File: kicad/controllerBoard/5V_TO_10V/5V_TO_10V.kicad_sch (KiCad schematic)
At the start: 35 parts, among them Q1 PMOS, Q636 PMOS, Q637 NMOS, Q638 NMOS, Q639 PMOS, Q640 NMOS, Q641 PMOS, Q642 NMOS, Q643 PMOS, Q644 NMOS, Q645 PMOS, Q646 NMOS, Q647 PMOS, Q648 NMOS

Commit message: did more simulation, added bom
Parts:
- removed D2: MUR1560F, Diode_THT:D_DO-35_SOD27_P7.62mm_Horizontal, symbol Device:D
- added D13, D14, D15, D16, D5: MUR1560FAC, Diode_THT:D_DO-35_SOD27_P7.62mm_Horizontal, symbol Device:D
- C16: renamed from C6; value 10mC -> 1mC
- D10, D11, D12, D7, D8, D9: value MUR1560F -> MUR1560FAC
- D6: renamed from D1; value MUR1560F -> MUR1560FAC
- renumbered C1 to C11, C2 to C12, C3 to C13, C4 to C14, C5 to C15, Q1 to Q635, R1 to R51, R2 to R52, R3 to R53, R4 to R54, R5 to R55, R6 to R56
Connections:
- net 10V: now also D16.1 (K); no longer D11.1 (K), D12.1 (K)
- net at D7.1 (K), D9.2 (A): no longer C14.1
- net at C12.1, D6.1 (K): now also D8.2 (A); no longer D7.2 (A)
- net at D10.2 (A), D8.1 (K): now also C14.1; no longer C15.1
- net at C13.1: no longer D8.2 (A)
- new net: D11.1 (K), D13.2 (A)
- new net: D12.1 (K), D14.2 (A)
- new net: D14.1 (K), D16.2 (A)
- new net: D5.1 (K), D7.2 (A)
- new net: D13.1 (K), D15.2 (A)
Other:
- moved on the sheet: C16

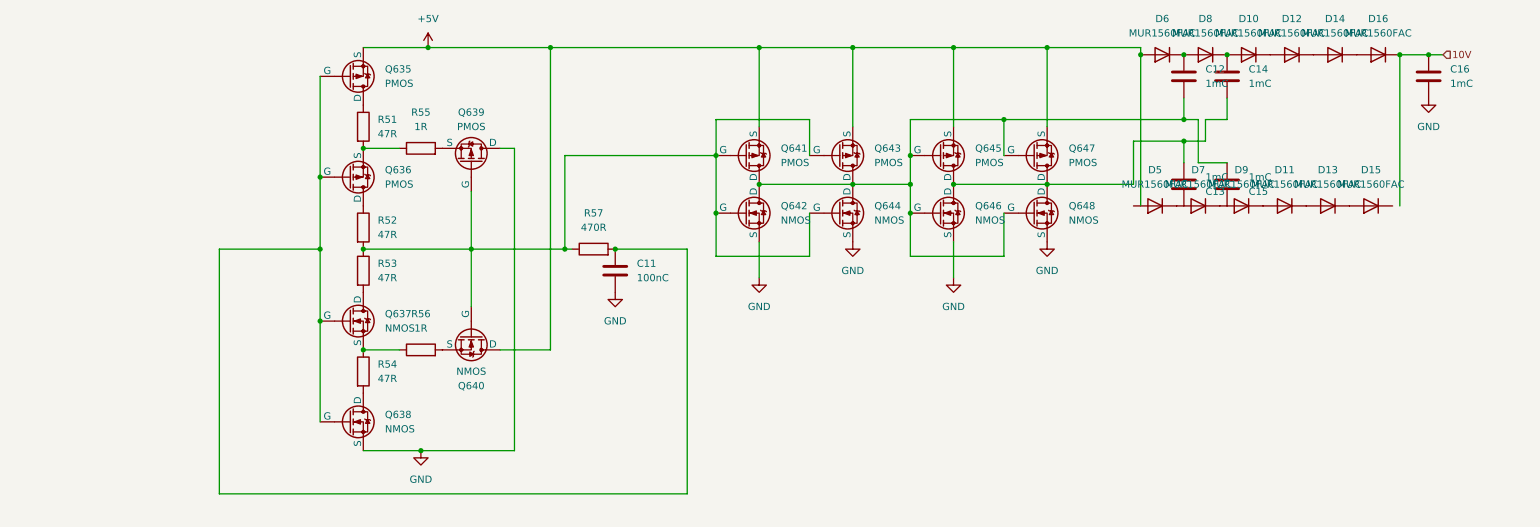
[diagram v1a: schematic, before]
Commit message: update main board schematic
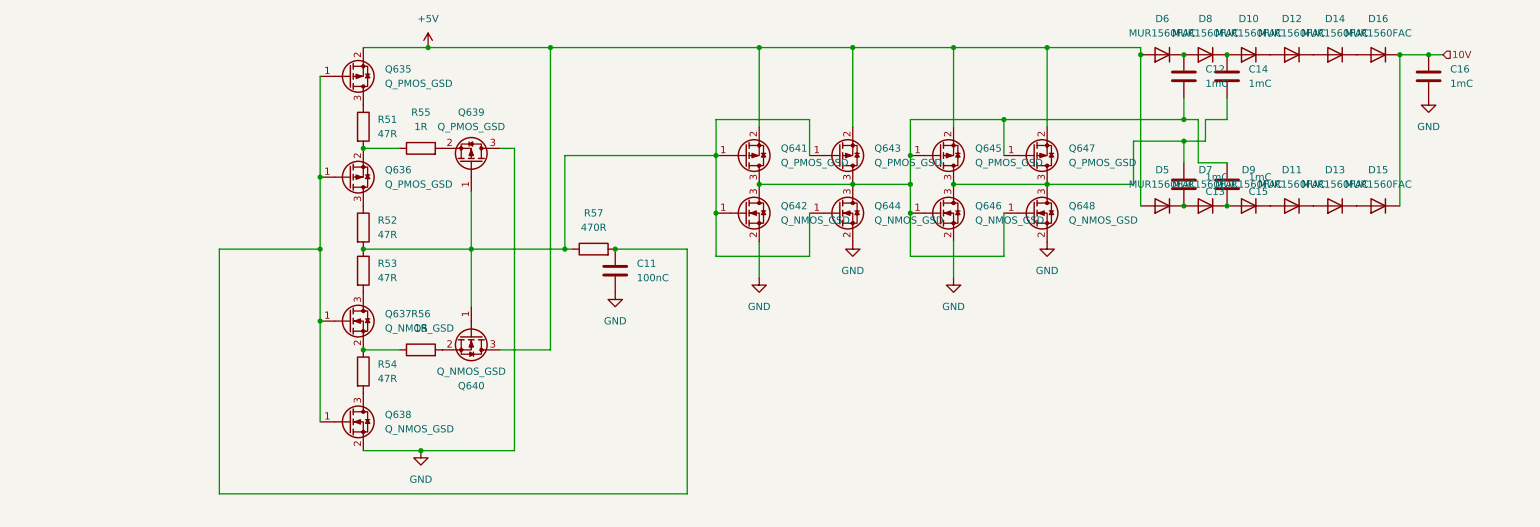
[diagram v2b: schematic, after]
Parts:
- C11: footprint (none) -> Capacitor_SMD:C_0805_2012Metric
- C12, C13, C14, C15, C16: footprint (none) -> Capacitor_THT:CP_Radial_D10.0mm_P5.00mm
- D10, D11, D12, D13, D14, D15, D16, D5, D6, D7, D8, D9: footprint Diode_THT:D_DO-35_SOD27_P7.62mm_Horizontal -> Package_TO_SOT_THT:TO-220-2_Vertical
- Q635, Q636, Q639, Q641, Q643, Q645, Q647: value PMOS -> Q_PMOS_GSD; footprint Package_DIP:DIP-24_W7.62mm -> easyeda2kicad:SOT-23-P; symbol Simulation_SPICE:PMOS -> Transistor_FET:Q_PMOS_GSD
- Q637, Q638, Q640, Q642, Q644, Q646, Q648: value NMOS -> Q_NMOS_GSD; footprint (none) -> easyeda2kicad:SOT-23-N; symbol Simulation_SPICE:NMOS -> Transistor_FET:Q_NMOS_GSD
- R51, R52, R53, R54, R55, R56, R57: footprint (none) -> Resistor_SMD:R_0805_2012Metric
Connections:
- net +5V: now also D5.2 (A), Q635.2 (S), Q640.3 (D), Q641.2 (S), Q643.2 (S), Q645.2 (S), Q647.2 (S); no longer Q635.3 (S), Q640.1 (D), Q641.3 (S), Q643.3 (S), Q645.3 (S), Q647.3 (S)
- net 10V: now also D15.1 (K)
- net GND: now also Q638.2 (S), Q639.3 (D), Q642.2 (S), Q644.2 (S), Q646.2 (S), Q648.2 (S); no longer Q638.3 (S), Q639.1 (D), Q642.3 (S), Q644.3 (S), Q646.3 (S), Q648.3 (S)
- net at Q645.1 (G), Q646.1 (G), Q647.1 (G)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: now also C12.2, C15.2, Q641.3 (D), Q642.3 (D), Q643.3 (D), Q644.3 (D); no longer C13.2, C14.2
- net at R54.1, R56.1: now also Q637.2 (S); no longer Q637.3 (S)
- net at R56.2: now also Q640.2 (S); no longer Q640.3 (S)
- net at Q636.1 (G): now also C11.1, Q635.1 (G), Q637.1 (G), Q638.1 (G), R57.2; no longer R52.1
- net at R51.2, R55.1: now also Q636.2 (S); no longer Q636.3 (S)
- net at R51.1: now also Q635.3 (D); no longer Q635.1 (D)
- net at R55.2: now also Q639.2 (S); no longer Q639.3 (S)
- net at C15.1: now also D7.1 (K), D9.2 (A)
- net at C13.1: now also D5.1 (K), D7.2 (A)
- net at R53.2: now also Q637.3 (D); no longer Q637.1 (D)
- net at R54.2: now also Q638.3 (D); no longer Q638.1 (D)
- new net: C13.2, C14.2, Q645.3 (D), Q646.3 (D), Q647.3 (D), Q648.3 (D)
- new net: Q639.1 (G), Q640.1 (G), Q641.1 (G), Q642.1 (G), Q643.1 (G), Q644.1 (G), R52.2, R53.1, R57.1
- new net: Q636.3 (D), R52.1
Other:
- moved on the sheet: D11, D13, D15, D5, D7, D9

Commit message: routed charge pump
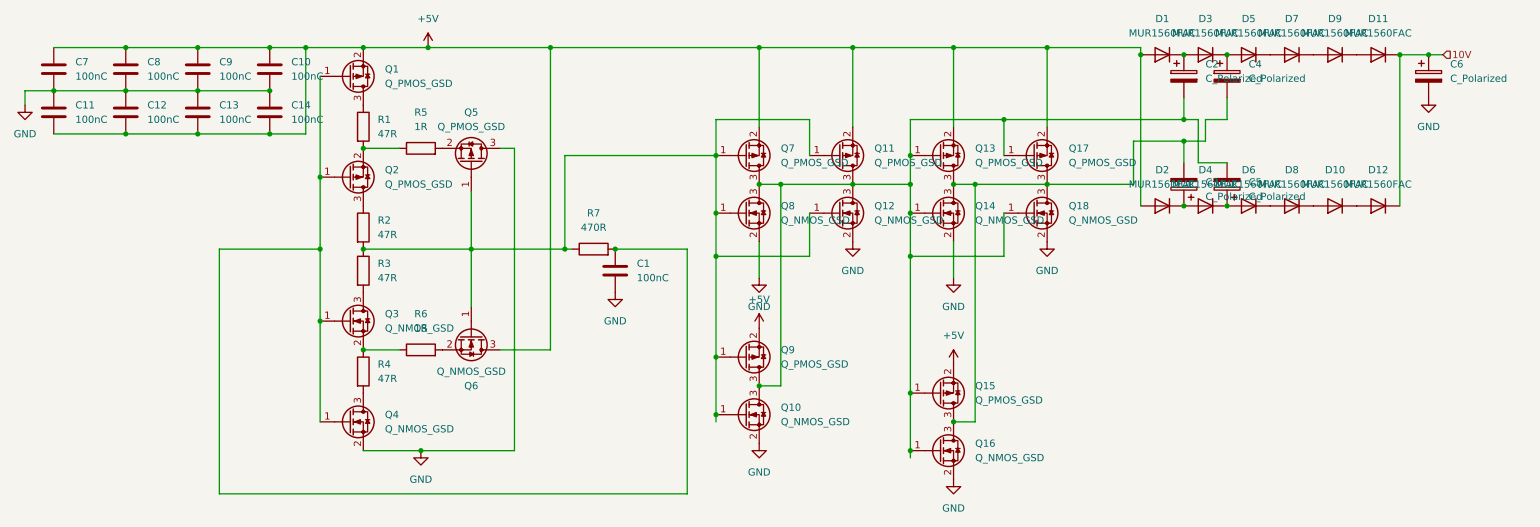
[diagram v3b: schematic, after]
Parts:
- removed C15, C16: 1mC, Capacitor_THT:CP_Radial_D10.0mm_P5.00mm, symbol Device:C
- added C10, C11, C7, C8, C9: 100nC, Capacitor_SMD:C_0805_2012Metric, symbol Device:C
- added C2, C3, C4, C5, C6: C_Polarized, Capacitor_THT:CP_Radial_D10.0mm_P5.00mm, symbol Device:C_Polarized
- added Q10, Q16: Q_NMOS_GSD, easyeda2kicad:SOT-23-N, symbol Transistor_FET:Q_NMOS_GSD
- added Q15, Q9: Q_PMOS_GSD, easyeda2kicad:SOT-23-P, symbol Transistor_FET:Q_PMOS_GSD
- C12, C13, C14: value 1mC -> 100nC; footprint Capacitor_THT:CP_Radial_D10.0mm_P5.00mm -> Capacitor_SMD:C_0805_2012Metric
- renumbered C11 to C1, D6 to D1, D13 to D10, D16 to D11, D15 to D12, D5 to D2, D8 to D3, D7 to D4, D10 to D5, D9 to D6, D12 to D7, D11 to D8, D14 to D9, Q635 to Q1, Q643 to Q11, Q644 to Q12, Q645 to Q13, Q646 to Q14, Q647 to Q17, Q648 to Q18, Q636 to Q2, Q637 to Q3, Q638 to Q4, Q639 to Q5, Q640 to Q6, Q641 to Q7, Q642 to Q8, R51 to R1, R52 to R2, R53 to R3, R54 to R4, R55 to R5, R56 to R6, R57 to R7
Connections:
- net +5V: now also C12.2, C13.2, C14.2, C10.1, C11.2, C7.1, C8.1, C9.1, Q15.2 (S), Q9.2 (S)
- net 10V: now also C6.1
- net GND: now also C12.1, C13.1, C14.1, C10.2, C11.1, C6.2, C7.2, C8.2, C9.2, Q10.2 (S), Q16.2 (S)
- net at Q11.3 (D), Q12.3 (D), Q13.1 (G)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: now also C2.2, C5.2, Q10.3 (D), Q15.1 (G), Q16.1 (G), Q9.3 (D); no longer C12.2
- net at Q13.3 (D), Q14.3 (D), Q17.3 (D)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: now also C3.2, C4.2, Q15.3 (D), Q16.3 (D); no longer C13.2, C14.2
- net at Q11.1 (G), Q12.1 (G), Q5.1 (G)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: now also Q10.1 (G), Q9.1 (G)
- net at D1.1 (K), D3.2 (A): now also C2.1; no longer C12.1
- net at D4.1 (K), D6.2 (A): now also C5.1
- net at D3.1 (K), D5.2 (A): now also C4.1; no longer C14.1
- net at D2.1 (K), D4.2 (A): now also C3.1; no longer C13.1

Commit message: finished routing all sub schematics
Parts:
- renumbered C7 to C17, C11 to C18, C8 to C19, C12 to C20, C9 to C21, C13 to C22, C10 to C23, C14 to C24, C1 to C25, C2 to C26, C3 to C27, C4 to C28, C5 to C29, C6 to C30, D6 to D10, D7 to D11, D8 to D12, D9 to D13, D10 to D14, D11 to D15, D12 to D16, D1 to D5, D2 to D6, D3 to D7, D4 to D8, D5 to D9, Q1 to Q635, Q2 to Q636, Q3 to Q637, Q4 to Q638, Q5 to Q639, Q6 to Q640, Q7 to Q641, Q8 to Q642, Q9 to Q643, Q10 to Q644, Q11 to Q645, Q12 to Q646, Q13 to Q647, Q14 to Q648, Q15 to Q649, Q16 to Q650, Q17 to Q651, Q18 to Q652, R1 to R51, R2 to R52, R3 to R53, R4 to R54, R5 to R55, R6 to R56, R7 to R57

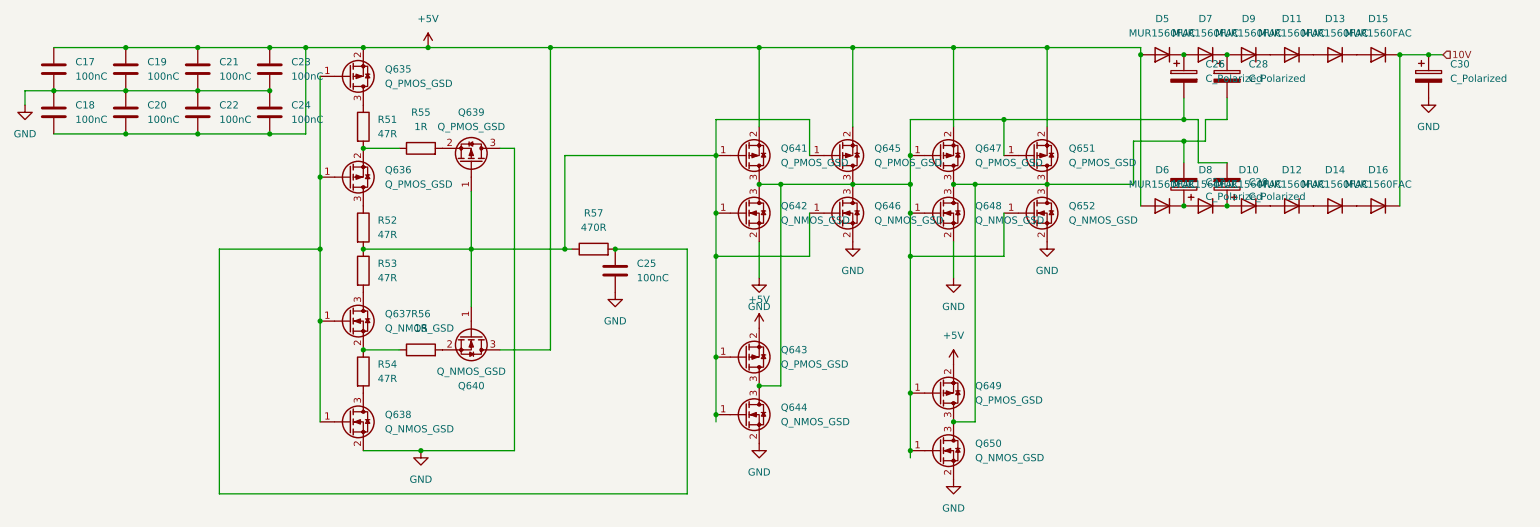
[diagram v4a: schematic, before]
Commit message: add mounting holes
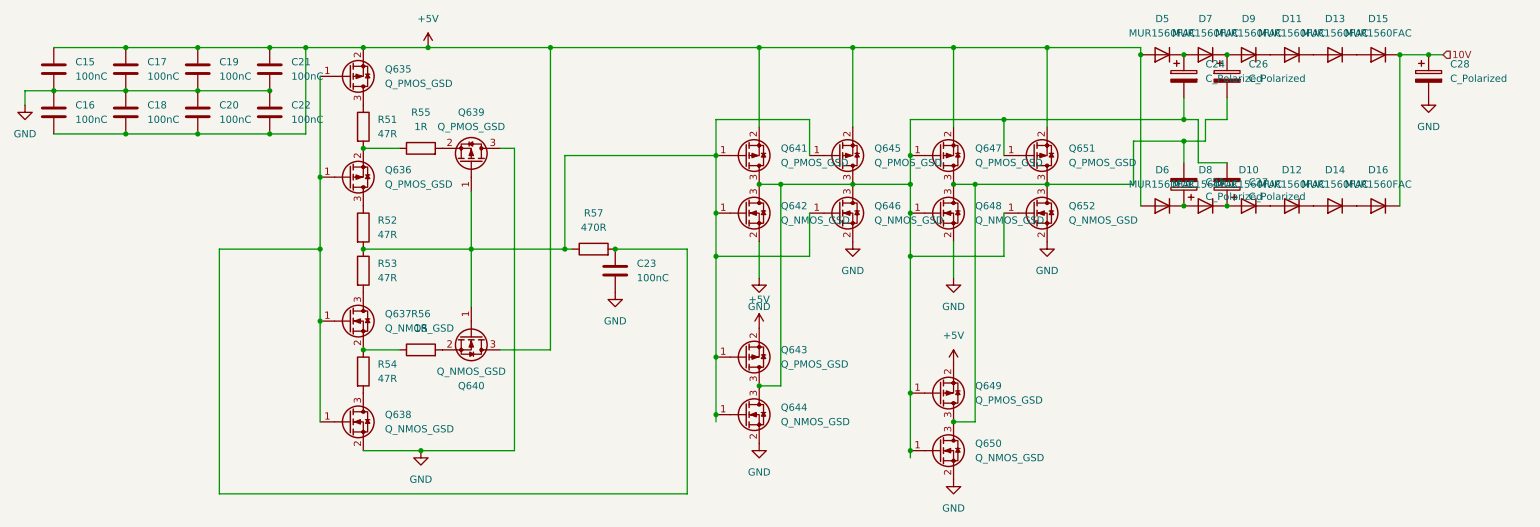
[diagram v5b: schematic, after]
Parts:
- renumbered C17 to C15, C18 to C16, C19 to C17, C20 to C18, C21 to C19, C22 to C20, C23 to C21, C24 to C22, C25 to C23, C26 to C24, C27 to C25, C28 to C26, C29 to C27, C30 to C28
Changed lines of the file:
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@@
 		(dnp no)
 		(fields_autoplaced yes)
-		(property "Reference" "#PWR0136"
+		(property "Reference" "#PWR0218"
 			(at 85.09 119.38 0)
 			(hide yes)
@@
 			(project "controllerBoard"
 				(path "/93a9a1ca-4ee5-40da-ab67-92836146c003/ba89c823-0b97-4162-9c8c-b0bfe5b1c3f2"
-					(reference "#PWR0136")
+					(reference "#PWR0218")
 					(unit 1)
 				)
@@
 		(dnp no)
 		(fields_autoplaced yes)
-		(property "Reference" "C23"
+		(property "Reference" "C21"
 			(at 62.23 44.4499 0)
 			(show_name no)
@@
 			(project "controllerBoard"
 				(path "/93a9a1ca-4ee5-40da-ab67-92836146c003/ba89c823-0b97-4162-9c8c-b0bfe5b1c3f2"
-					(reference "C23")
+					(reference "C21")
 					(unit 1)
 				)
@@
 		(dnp no)
 		(fields_autoplaced yes)
-		(property "Reference" "C30"
+		(property "Reference" "C28"
 			(at 266.7 44.8309 0)
 			(show_name no)
@@
 			(project "controllerBoard"
 				(path "/93a9a1ca-4ee5-40da-ab67-92836146c003/ba89c823-0b97-4162-9c8c-b0bfe5b1c3f2"
-					(reference "C30")
+					(reference "C28")
 					(unit 1)
 				)
@@
 		(dnp no)
 		(fields_autoplaced yes)
-		(property "Reference" "C25"
+		(property "Reference" "C23"
 			(at 123.19 80.0099 0)
 			(show_name no)
@@
 			(project "controllerBoard"
 				(path "/93a9a1ca-4ee5-40da-ab67-92836146c003/ba89c823-0b97-4162-9c8c-b0bfe5b1c3f2"
-					(reference "C25")
+					(reference "C23")
 					(unit 1)
 				)
@@
 		(dnp no)
 		(fields_autoplaced yes)
-		(property "Reference" "#PWR0146"
+		(property "Reference" "#PWR0228"
 			(at 195.58 82.55 0)
 			(hide yes)
@@
 			(project "controllerBoard"
 				(path "/93a9a1ca-4ee5-40da-ab67-92836146c003/ba89c823-0b97-4162-9c8c-b0bfe5b1c3f2"
-					(reference "#PWR0146")
+					(reference "#PWR0228")
 					(unit 1)
 				)
@@
 		(dnp no)
 		(fields_autoplaced yes)
-		(property "Reference" "#PWR0135"
+		(property "Reference" "#PWR0217"
 			(at 15.24 58.42 0)
 			(hide yes)
@@
 			(project "controllerBoard"
 				(path "/93a9a1ca-4ee5-40da-ab67-92836146c003/ba89c823-0b97-4162-9c8c-b0bfe5b1c3f2"
-					(reference "#PWR0135")
+					(reference "#PWR0217")
 					(unit 1)
 				)
@@
 		(dnp no)
 		(fields_autoplaced yes)
-		(property "Reference" "C17"
+		(property "Reference" "C15"
 			(at 24.13 44.4499 0)
 			(show_name no)
@@
 			(project "controllerBoard"
 				(path "/93a9a1ca-4ee5-40da-ab67-92836146c003/ba89c823-0b97-4162-9c8c-b0bfe5b1c3f2"
-					(reference "C17")
+					(reference "C15")
 					(unit 1)
 				)
@@
 		(dnp no)
 		(fields_autoplaced yes)
-		(property "Reference" "#PWR0142"
+		(property "Reference" "#PWR0224"
 			(at 161.29 82.55 0)
 			(hide yes)
@@
 			(project "controllerBoard"
 				(path "/93a9a1ca-4ee5-40da-ab67-92836146c003/ba89c823-0b97-4162-9c8c-b0bfe5b1c3f2"
-					(reference "#PWR0142")
+					(reference "#PWR0224")
 					(unit 1)
 				)
@@
 		(dnp no)
 		(fields_autoplaced yes)
-		(property "Reference" "C20"
+		(property "Reference" "C18"
 			(at 36.83 52.0699 0)
 			(show_name no)
@@
 			(project "controllerBoard"
 				(path "/93a9a1ca-4ee5-40da-ab67-92836146c003/ba89c823-0b97-4162-9c8c-b0bfe5b1c3f2"
-					(reference "C20")
+					(reference "C18")
 					(unit 1)
 				)
@@
 		(dnp no)
 		(fields_autoplaced yes)
-		(property "Reference" "C27"
+		(property "Reference" "C25"
 			(at 223.52 65.6589 0)
 			(show_name no)
@@
 			(project "controllerBoard"
 				(path "/93a9a1ca-4ee5-40da-ab67-92836146c003/ba89c823-0b97-4162-9c8c-b0bfe5b1c3f2"
-					(reference "C27")
+					(reference "C25")
 					(unit 1)
 				)
@@
 		(dnp no)
 		(fields_autoplaced yes)
-		(property "Reference" "#PWR0139"
+		(property "Reference" "#PWR0221"
 			(at 144.78 88.9 0)
 			(hide yes)
@@
 			(project "controllerBoard"
 				(path "/93a9a1ca-4ee5-40da-ab67-92836146c003/ba89c823-0b97-4162-9c8c-b0bfe5b1c3f2"
-					(reference "#PWR0139")
+					(reference "#PWR0221")
 					(unit 1)
 				)
@@
 		(dnp no)
 		(fields_autoplaced yes)
-		(property "Reference" "C18"
+		(property "Reference" "C16"
 			(at 24.13 52.0699 0)
 			(show_name no)
@@
 			(project "controllerBoard"
 				(path "/93a9a1ca-4ee5-40da-ab67-92836146c003/ba89c823-0b97-4162-9c8c-b0bfe5b1c3f2"
-					(reference "C18")
+					(reference "C16")
 					(unit 1)
 				)
@@
 		(dnp no)
 		(fields_autoplaced yes)
-		(property "Reference" "C28"
+		(property "Reference" "C26"
 			(at 231.14 44.8309 0)
 			(show_name no)
@@
 			(project "controllerBoard"
 				(path "/93a9a1ca-4ee5-40da-ab67-92836146c003/ba89c823-0b97-4162-9c8c-b0bfe5b1c3f2"
-					(reference "C28")
+					(reference "C26")
 					(unit 1)
 				)
@@
 		(dnp no)
 		(fields_autoplaced yes)
-		(property "Reference" "C29"
+		(property "Reference" "C27"
 			(at 231.14 65.6589 0)
 			(show_name no)
@@
 			(project "controllerBoard"
 				(path "/93a9a1ca-4ee5-40da-ab67-92836146c003/ba89c823-0b97-4162-9c8c-b0bfe5b1c3f2"
-					(reference "C29")
+					(reference "C27")
 					(unit 1)
 				)
@@
 		(dnp no)
 		(fields_autoplaced yes)
-		(property "Reference" "#PWR0147"
+		(property "Reference" "#PWR0229"
 			(at 262.89 57.15 0)
 			(hide yes)
@@
 			(project "controllerBoard"
 				(path "/93a9a1ca-4ee5-40da-ab67-92836146c003/ba89c823-0b97-4162-9c8c-b0bfe5b1c3f2"
-					(reference "#PWR0147")
+					(reference "#PWR0229")
 					(unit 1)
 				)
@@
 		(dnp no)
 		(fields_autoplaced yes)
-		(property "Reference" "#PWR0140"
+		(property "Reference" "#PWR0222"
 			(at 144.78 95.25 0)
 			(hide yes)
@@
 			(project "controllerBoard"
 				(path "/93a9a1ca-4ee5-40da-ab67-92836146c003/ba89c823-0b97-4162-9c8c-b0bfe5b1c3f2"
-					(reference "#PWR0140")
+					(reference "#PWR0222")
 					(unit 1)
 				)
@@
 		(dnp no)
 		(fields_autoplaced yes)
-		(property "Reference" "C21"
+		(property "Reference" "C19"
 			(at 49.53 44.4499 0)
 			(show_name no)
@@
 			(project "controllerBoard"
 				(path "/93a9a1ca-4ee5-40da-ab67-92836146c003/ba89c823-0b97-4162-9c8c-b0bfe5b1c3f2"
-					(reference "C21")
+					(reference "C19")
 					(unit 1)
 				)
@@
 		(dnp no)
 		(fields_autoplaced yes)
-		(property "Reference" "#PWR0137"
+		(property "Reference" "#PWR0219"
 			(at 86.36 45.72 0)
 			(hide yes)
@@
 			(project "controllerBoard"
 				(path "/93a9a1ca-4ee5-40da-ab67-92836146c003/ba89c823-0b97-4162-9c8c-b0bfe5b1c3f2"
-					(reference "#PWR0137")
+					(reference "#PWR0219")
 					(unit 1)
 				)
@@
 		(dnp no)
 		(fields_autoplaced yes)
-		(property "Reference" "#PWR0145"
+		(property "Reference" "#PWR0227"
 			(at 179.07 124.46 0)
 			(hide yes)
@@
 			(project "controllerBoard"
 				(path "/93a9a1ca-4ee5-40da-ab67-92836146c003/ba89c823-0b97-4162-9c8c-b0bfe5b1c3f2"
-					(reference "#PWR0145")
+					(reference "#PWR0227")
 					(unit 1)
 				)
@@
 		(dnp no)
 		(fields_autoplaced yes)
-		(property "Reference" "C26"
+		(property "Reference" "C24"
 			(at 223.52 44.8309 0)
 			(show_name no)
@@
 			(project "controllerBoard"
 				(path "/93a9a1ca-4ee5-40da-ab67-92836146c003/ba89c823-0b97-4162-9c8c-b0bfe5b1c3f2"
-					(reference "C26")
+					(reference "C24")
 					(unit 1)
 				)
@@
 		(dnp no)
 		(fields_autoplaced yes)
-		(property "Reference" "#PWR0143"
+		(property "Reference" "#PWR0225"
 			(at 179.07 88.9 0)
 			(hide yes)
@@
 			(project "controllerBoard"
 				(path "/93a9a1ca-4ee5-40da-ab67-92836146c003/ba89c823-0b97-4162-9c8c-b0bfe5b1c3f2"
-					(reference "#PWR0143")
+					(reference "#PWR0225")
 					(unit 1)
 				)
@@
 		(dnp no)
 		(fields_autoplaced yes)
-		(property "Reference" "C19"
+		(property "Reference" "C17"
 			(at 36.83 44.4499 0)
 			(show_name no)
@@
 			(project "controllerBoard"
 				(path "/93a9a1ca-4ee5-40da-ab67-92836146c003/ba89c823-0b97-4162-9c8c-b0bfe5b1c3f2"
-					(reference "C19")
+					(reference "C17")
 					(unit 1)
 				)
@@
 		(dnp no)
 		(fields_autoplaced yes)
-		(property "Reference" "#PWR0141"
+		(property "Reference" "#PWR0223"
 			(at 144.78 118.11 0)
 			(hide yes)
@@
 			(project "controllerBoard"
 				(path "/93a9a1ca-4ee5-40da-ab67-92836146c003/ba89c823-0b97-4162-9c8c-b0bfe5b1c3f2"
-					(reference "#PWR0141")
+					(reference "#PWR0223")
 					(unit 1)
 				)
@@
 		(dnp no)
 		(fields_autoplaced yes)
-		(property "Reference" "#PWR0144"
+		(property "Reference" "#PWR0226"
 			(at 179.07 101.6 0)
 			(hide yes)
@@
 			(project "controllerBoard"
 				(path "/93a9a1ca-4ee5-40da-ab67-92836146c003/ba89c823-0b97-4162-9c8c-b0bfe5b1c3f2"
-					(reference "#PWR0144")
+					(reference "#PWR0226")
 					(unit 1)
 				)
@@
 		(dnp no)
 		(fields_autoplaced yes)
-		(property "Reference" "C22"
+		(property "Reference" "C20"
 			(at 49.53 52.0699 0)
 			(show_name no)
@@
 			(project "controllerBoard"
 				(path "/93a9a1ca-4ee5-40da-ab67-92836146c003/ba89c823-0b97-4162-9c8c-b0bfe5b1c3f2"
-					(reference "C22")
+					(reference "C20")
 					(unit 1)
 				)
@@
 		(dnp no)
 		(fields_autoplaced yes)
-		(property "Reference" "C24"
+		(property "Reference" "C22"
 			(at 62.23 52.0699 0)
 			(show_name no)
@@
 			(project "controllerBoard"
 				(path "/93a9a1ca-4ee5-40da-ab67-92836146c003/ba89c823-0b97-4162-9c8c-b0bfe5b1c3f2"
-					(reference "C24")
+					(reference "C22")
 					(unit 1)
 				)
@@
 		(dnp no)
 		(fields_autoplaced yes)
-		(property "Reference" "#PWR0138"
+		(property "Reference" "#PWR0220"
 			(at 119.38 91.44 0)
 			(hide yes)
@@
 			(project "controllerBoard"
 				(path "/93a9a1ca-4ee5-40da-ab67-92836146c003/ba89c823-0b97-4162-9c8c-b0bfe5b1c3f2"
-					(reference "#PWR0138")
+					(reference "#PWR0220")
 					(unit 1)
 				)
